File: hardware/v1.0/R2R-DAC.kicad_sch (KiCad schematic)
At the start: 15 parts, among them U1 74LVC245A

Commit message: backup
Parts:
- removed RN10, RN3, RN4, RN5, RN6, RN9: 270, Resistor_SMD:R_Array_Convex_4x0603, symbol Device:R_Pack04_Split
- added unit 2 of RN7
- added unit 3 of RN7
- added unit 4 of RN7
- added unit 4 of RN8
- added unit 2 of RN8
- added unit 3 of RN8
- renumbered C2 to C?, C1 to C?, R1 to R?, R2 to R?, RN1 to RN?, RN2 to RN?, U1 to U?
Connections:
- net ANALOG_OUT: now also RN8.1 (R1.1)
- net at RN?.1 (R1.1): now also RN8.8 (R1.2), RN8.2 (R2.1)
- net at RN?.2 (R2.1): now also RN8.3 (R3.1), RN8.7 (R2.2); no longer RN8.1 (R1.1)
- net at RN?.1 (R1.1): now also RN7.8 (R1.2), RN7.2 (R2.1)
- net at RN?.2 (R2.1): now also RN7.3 (R3.1), RN7.7 (R2.2)
- net at RN?.3 (R3.1): now also RN7.4 (R4.1), RN7.6 (R3.2)
- net at R?.2, RN?.4 (R4.1): now also RN7.5 (R4.2)
- net at RN?.4 (R4.1): now also RN7.1 (R1.1), RN8.5 (R4.2); no longer RN7.8 (R1.2)
- new net: RN8.4 (R4.1), RN8.6 (R3.2), RN?.3 (R3.1)

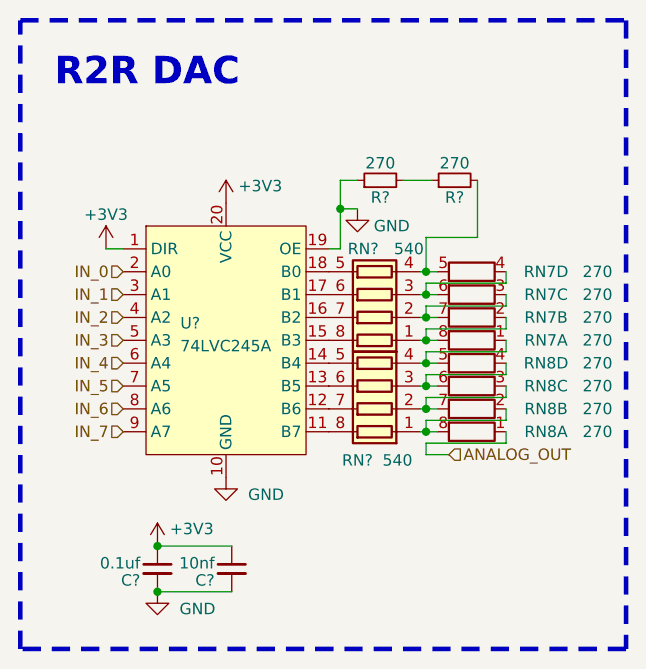
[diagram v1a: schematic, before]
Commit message: updated project to Kicad version 9.0
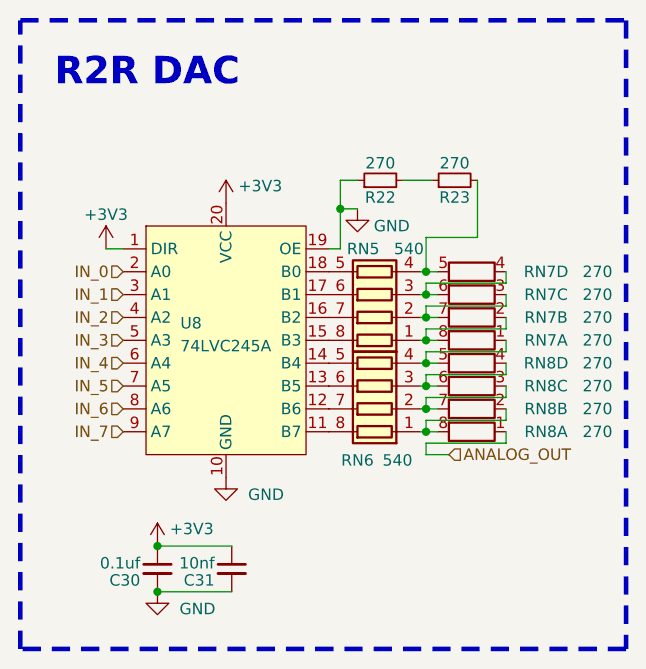
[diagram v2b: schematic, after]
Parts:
- gave numbers to parts that had none: 7

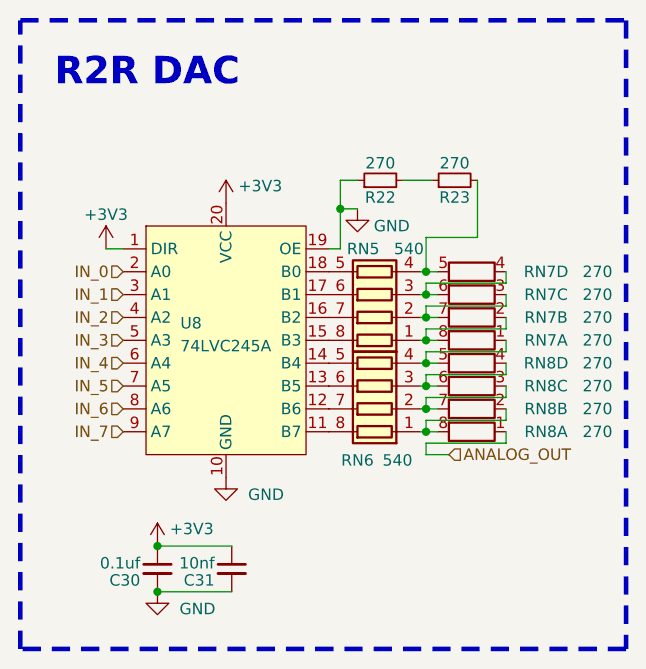
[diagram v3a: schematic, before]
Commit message: added tvs diode+changed inductors
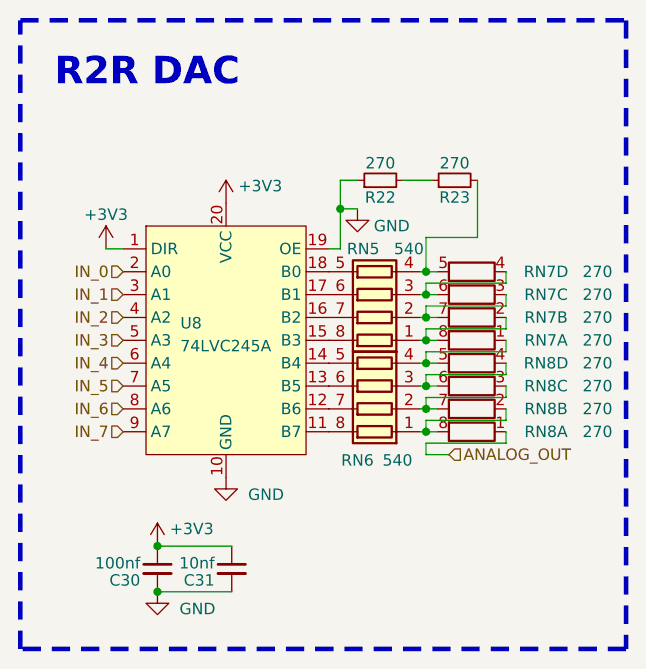
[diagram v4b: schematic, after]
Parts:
- C30: value 0.1uf -> 100nf
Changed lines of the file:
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@@
 			)
 		)
-		(property "Value" "0.1uf"
+		(property "Value" "100nf"
 			(at 27.94 75.565 0)
 			(effects
